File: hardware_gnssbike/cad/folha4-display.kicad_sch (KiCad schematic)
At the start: 11 parts, among them J401 Hirose FH12-10S-0.5SH(55), J402 Molex 503480-0500, Q401 DMG1012T-7

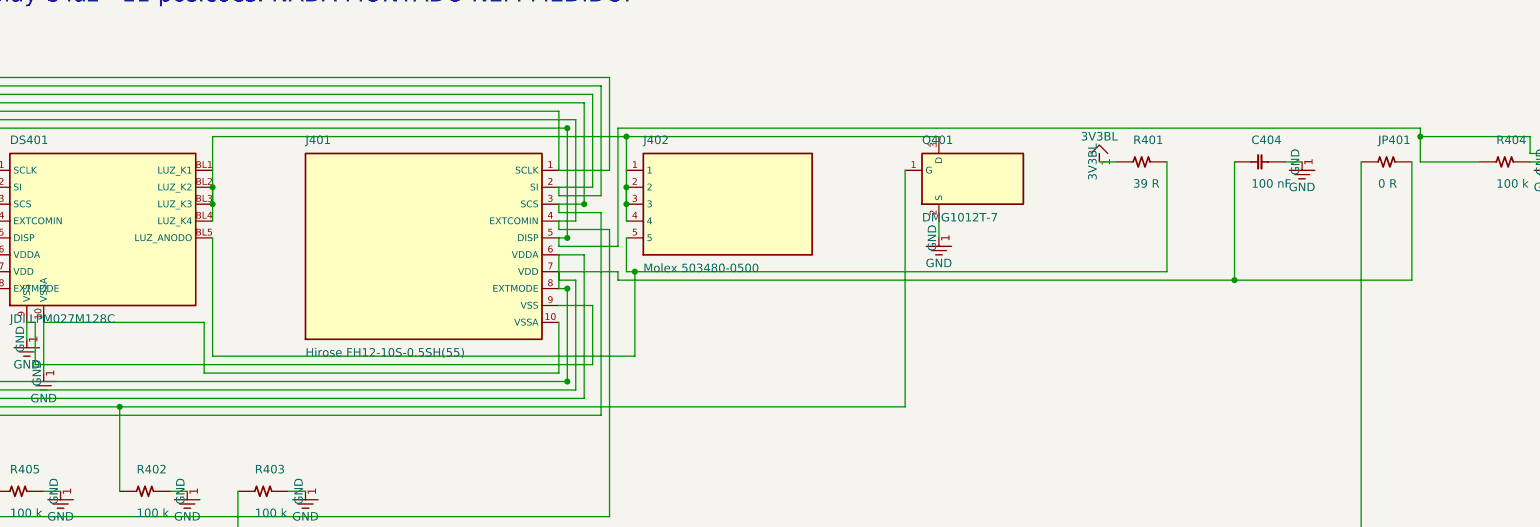
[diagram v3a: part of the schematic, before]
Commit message: feat(hardware): real symbols and real 3D models, from KiCad's own libraries
Two of the owner's asks in one commit, because they turned out to be the
same idea: stop drawing what already exists, reviewed, in the library.

THE SCHEMATIC. 36 of the parts were rectangles with pins around them - the
ICs, the connectors and the display - and a rectangle says nothing. Anyone
reading a schematic recognises a coaxial connector by the circle with the
dot, a switch by the contact that opens, a MOSFET by the channel and the
arrow.

ksym.py reads a symbol out of KiCad's own library - 21.110 of them, every
one reviewed against the KLC - and embeds it in our schematic with our
properties. simbolos.py says which part uses which. Eleven are in, and
ksym.checar() verifies every one pin number by pin number, because a
pretty symbol with the wire on the wrong pin is worse than a correct
rectangle. RF_GPS:MAX-M10S is literally our receiver: 18 pins, 18 names,
the same LCC-18.

Three symbols verify clean and still break the drawing, and they are
parked with the reason MEASURED rather than "did not work": the ADP5091
puts MPPT on the bottom edge beside its three ground pins and the ground
power symbol lands on the MPPT wire; the USB-C stacks four contacts per
point with 5,08 mm stubs and VBUS meets CC1; the ten pins of the display
FPC are all on one edge and two wires cannot reach. Each needs work
somewhere else - the power symbol placer, the placement - not a different
symbol.

Three bugs were found and fixed on the way, all in the router, all of the
same family: it assumed things about symbols that are only true of the
ones this project draws.

  - Symbols from KiCad are NOT centred on their origin. A
    Conn_01x10_Socket has its drawing at x -1,27 to 0 and all ten pins at
    x = -5,08. Treated as centred, pins fall inside the obstacle, the
    router cannot reach them from outside and goes over them instead -
    and two nets that touch are one net, with nothing in the drawing
    sa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
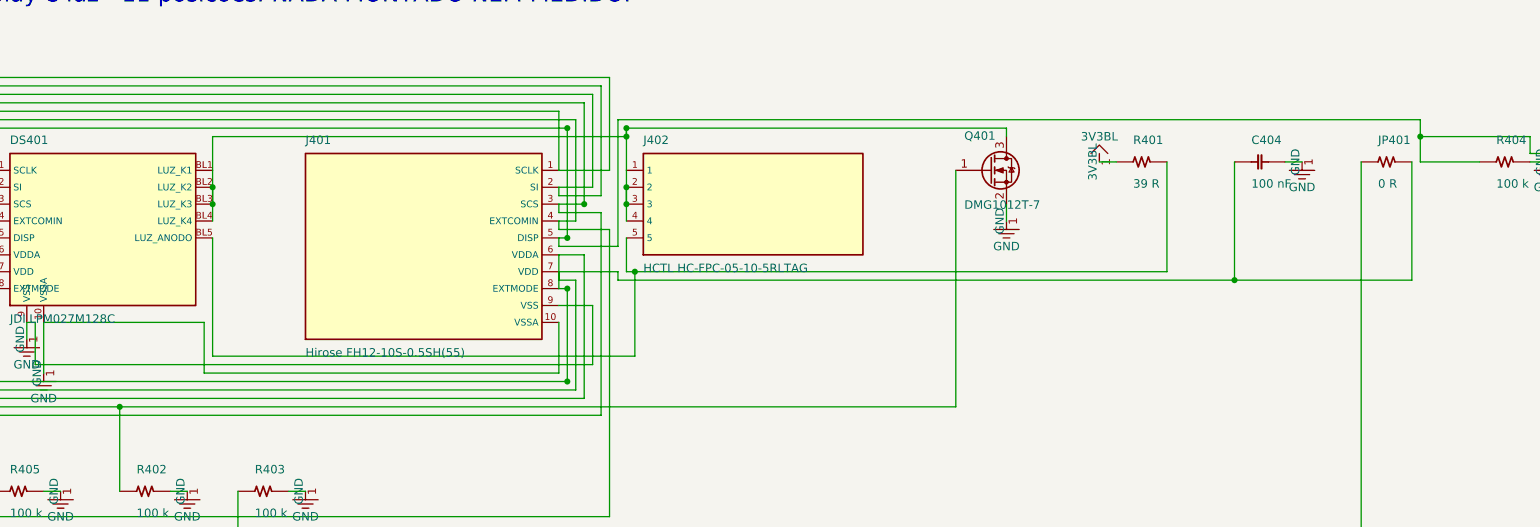
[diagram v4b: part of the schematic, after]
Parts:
- J402: value Molex 503480-0500 -> HCTL HC-FPC-05-10-5RLTAG; footprint Connector_FFC-FPC:TE_0-1734839-5_1x05-1MP_P0.5mm_Horizontal -> gnssbike:HC-FPC-05-10-5RLTAG
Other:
- moved on the sheet: J402
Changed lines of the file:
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@@
 	(wire
 		(pts
-			(xy 171.450 44.450) (xy 171.450 46.990)
+			(xy 181.610 41.910) (xy 181.610 44.450)
 		)
 		(stroke (width 0) (type default))
@@
 	(wire
 		(pts
-			(xy 124.460 31.750) (xy 171.450 31.750)
-		)
-		(stroke (width 0) (type default))
-	)
-	(wire
-		(pts
-			(xy 124.460 31.750) (xy 124.460 36.830)
+			(xy 181.610 30.480) (xy 181.610 31.750)
+		)
+		(stroke (width 0) (type default))
+	)
+	(wire
+		(pts
+			(xy 124.460 30.480) (xy 181.610 30.480)
+		)
+		(stroke (width 0) (type default))
+	)
+	(wire
+		(pts
+			(xy 124.460 31.750) (xy 124.460 30.480)
+		)
+		(stroke (width 0) (type default))
+	)
+	(wire
+		(pts
+			(xy 124.460 30.480) (xy 124.460 36.830)
 		)
 		(stroke (width 0) (type default))
@@
 	(wire
 		(pts
-			(xy 48.260 72.390) (xy 166.370 72.390)
-		)
-		(stroke (width 0) (type default))
-	)
-	(wire
-		(pts
-			(xy 166.370 36.830) (xy 166.370 72.390)
+			(xy 48.260 72.390) (xy 173.990 72.390)
+		)
+		(stroke (width 0) (type default))
+	)
+	(wire
+		(pts
+			(xy 173.990 36.830) (xy 173.990 72.390)
 		)
 		(stroke (width 0) (type default))
@@
 	(wire
 		(pts
-			(xy 243.840 30.480) (xy 243.840 31.750)
+			(xy 243.840 29.210) (xy 243.840 31.750)
 		)
 		(stroke (width 0) (type default))
@@
 	(wire
 		(pts
-			(xy 123.190 30.480) (xy 243.840 30.480)
-		)
-		(stroke (width 0) (type default))
-	)
-	(wire
-		(pts
-			(xy 123.190 30.480) (xy 123.190 48.260)
+			(xy 123.190 29.210) (xy 243.840 29.210)
+		)
+		(stroke (width 0) (type default))
+	)
+	(wire
+		(pts
+			(xy 123.190 29.210) (xy 123.190 48.260)
 		)
 		(stroke (width 0) (type default))
@@
 	(junction
 		(at 124.460 41.910)
+		(diameter 0)
+		(color 0 0 0 0)
+	)
+	(junction
+		(at 124.460 30.480)
 		(diameter 0)
 		(color 0 0 0 0)
@@
 	(symbol
 		(lib_id "gnssbike:J402")
-		(at 139.700 41.910 0)
+		(at 143.510 41.910 0)
 		(unit 1)
 		(exclude_from_sim no)
@@
 			(effects (font (size 1.27 1.27)) (justify left bottom))
 		)
-		(property "Value" "Molex 503480-0500"
+		(property "Value" "HCTL HC-FPC-05-10-5RLTAG"
 			(at 127.000 50.800 0)
 			(effects (font (size 1.27 1.27)) (justify left top))
 		)
-		(property "Footprint" "Connector_FFC-FPC:TE_0-1734839-5_1x05-1MP_P0.5mm_Horizontal"
-			(at 139.7 41.910000000000004 0)
+		(property "Footprint" "gnssbike:HC-FPC-05-10-5RLTAG"
+			(at 143.51 41.910000000000004 0)
 			(effects (font (size 1.27 1.27)) (hide yes))
 		)
 		(property "Datasheet" ""
-			(at 139.7 41.910000000000004 0)
+			(at 143.51 41.910000000000004 0)
 			(effects (font (size 1.27 1.27)) (hide yes))
 		)
 		(property "Description" "conector da luz do painel, 5 vias, passo 0,5 mm, recomendado pela propria JDI no desenho de contorno"
-			(at 139.7 41.910000000000004 0)
+			(at 143.51 41.910000000000004 0)
 			(effects (font (size 1.27 1.27)) (hide yes))
 		)
@@
 	(symbol
 		(lib_id "gnssbike:Q401")
-		(at 176.530 38.100 0)
+		(at 179.070 36.830 0)
 		(unit 1)
 		(exclude_from_sim no)
@@
 		(dnp no)
 		(property "Reference" "Q401"
-			(at 168.910 33.020 0)
+			(at 175.260 32.385 0)
 			(effects (font (size 1.27 1.27)) (justify left bottom))
 		)
 		(property "Value" "DMG1012T-7"
-			(at 168.910 43.180 0)
+			(at 175.260 41.275 0)
 			(effects (font (size 1.27 1.27)) (justify left top))
 		)
 		(property "Footprint" "Package_TO_SOT_SMD:SOT-523"
-			(at 176.53 38.1 0)
+			(at 179.07 36.83 0)
 			(effects (font (size 1.27 1.27)) (hide yes))
 		)
 		(property "Datasheet" ""
-			(at 176.53 38.1 0)
+			(at 179.07 36.83 0)
 			(effects (font (size 1.27 1.27)) (hide yes))
 		)
 		(property "Description" "chave de canal N da luz. A Diodes NAO publica numero de pino: o diagrama so mostra a posicao, e a numeracao vem do padrao SOT-523 | PINAGEM NAO CONFIRMADA NA FICHA"
-			(at 176.53 38.1 0)
+			(at 179.07 36.83 0)
 			(effects (font (size 1.27 1.27)) (hide yes))
 		)
@@
 	(symbol
 		(lib_id "power:GND")
-		(at 171.450 46.990 0)
+		(at 181.610 44.450 0)
 		(unit 1)
 		(exclude_from_sim no)
@@
 		(dnp no)
 		(property "Reference" "#PWR003"
-			(at 171.45 46.99 0)
+			(at 181.61 44.449999999999996 0)
 			(effects (font (size 1.27 1.27)) (hide yes))
 		)
 		(property "Value" "GND"
-			(at 171.450 50.800 0)
+			(at 181.610 48.260 0)
 			(effects (font (size 1.27 1.27)))
 		)
 		(property "Footprint" ""
-			(at 171.45 46.99 0)
+			(at 181.61 44.449999999999996 0)
 			(effects (font (size 1.27 1.27)) (hide yes))
 		)
 		(property "Datasheet" ""
-			(at 171.45 46.99 0)
-			(effects (font (size 1.27 1.27)) (hide yes))
-		)
+			(at 181.61 44.449999999999996 0)
+			(effects (font (size 1.27 1.27)) (hide yes))
+		)

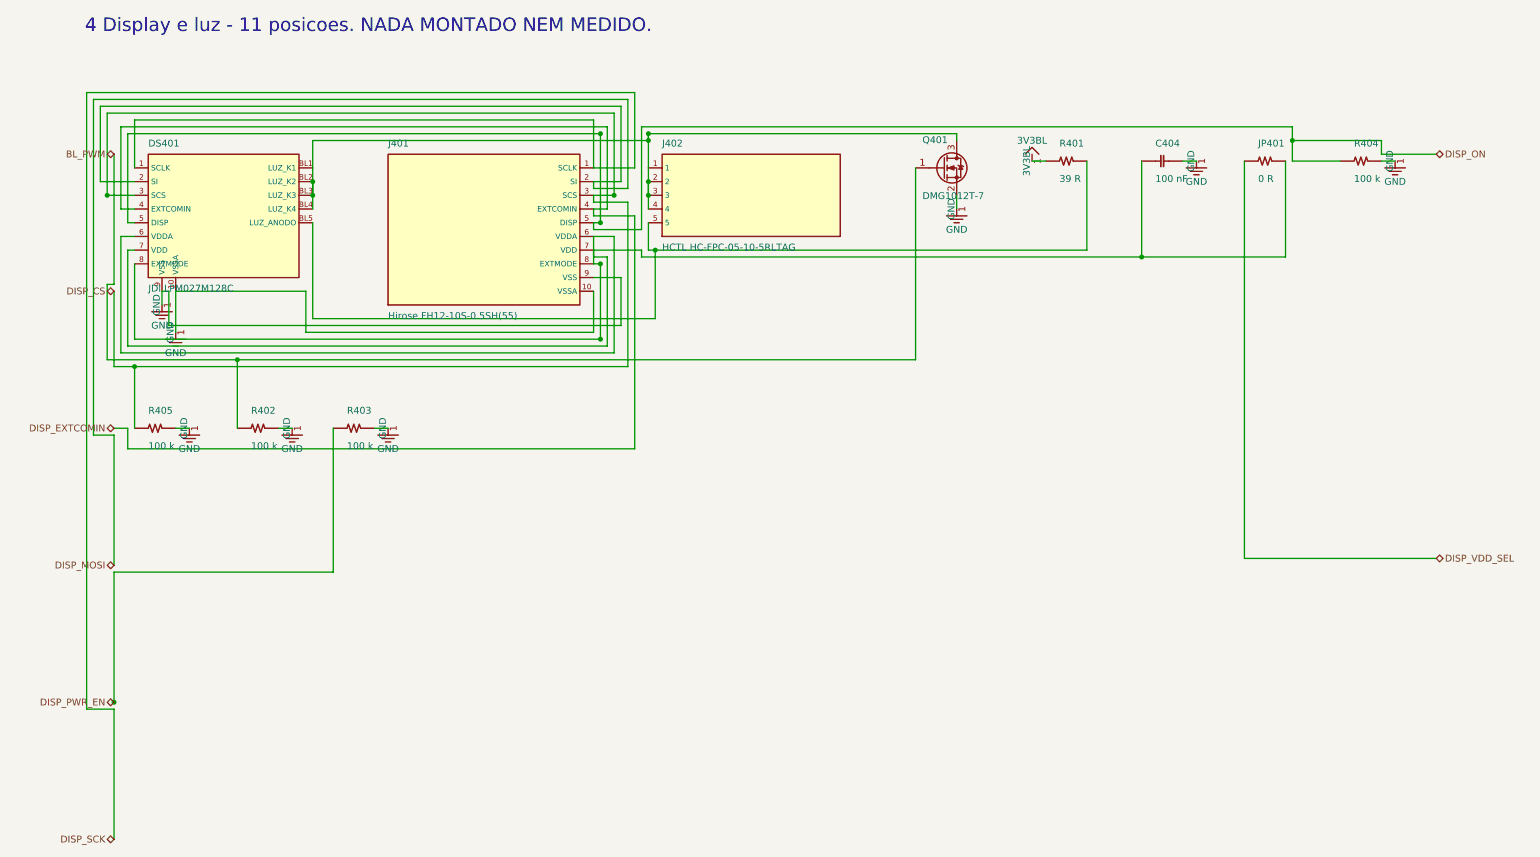
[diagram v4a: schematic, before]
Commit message: fix(hardware): the debug connector had RESET on the wrong contact
This one would have cost a board. The Tag-Connect TC2030 footprint had
pin 3 as no-connect and RESET on pin 6. The manufacturer's own data
sheet, TC2030-CTX_1.pdf, table "Connections", says the opposite: on the
six-pin footprint it is 3 = nRESET and 6 = SWO/TDO.

Where the mistake came from is worth writing down, because it is easy to
make twice: 1 VCC, 2 SWDIO, 3 GND, 4 SWCLK, 5 GND, 6 SWO is the
numbering of the ten-way Cortex header on the PROBE side, not of the
six-pin footprint on the board. Mixing the two gives exactly what was
written here.

What it would have done: the probe's nRESET is an open drain output, so
it would have driven nothing, and the MCU's reset would have hung off
the probe's SWO INPUT. Nothing burns - SWO runs target to probe, there
is no short - but the debugger can never reset the target: no connect
under reset, no pin reset. On an nRF54LM20A that reboots from task_wdt
or reconfigures its SWD pins, that removes the standard way out and
leaves only a full CTRL-AP erase.

The documentation carried a worse version still. 06 had GND on contact 3,
which fabricated would tie the probe's open-drain nRESET to copper
ground and hold the target in reset forever.

The project's own notes had predicted this exact variant - 06 carried a
CAUTION saying so and README an open checklist item. It was that one, and
it was caught before layout. Both are now closed, and the connector's
pin 6 is recorded as SWO with what is still unknown about it: which pad
of the ME54BS13 exposes SWO, which would give printf over ITM during
bring-up.

Fixed in parts.py, nets.py, 03-netlist.md, 06-conectores-e-pontos-de-teste.md,
07-sequencias-e-protecao.md and README.md.

Verified: check_sch and check_pcb pass, 78 of 78 diagrams render, 1529
links and none broken.
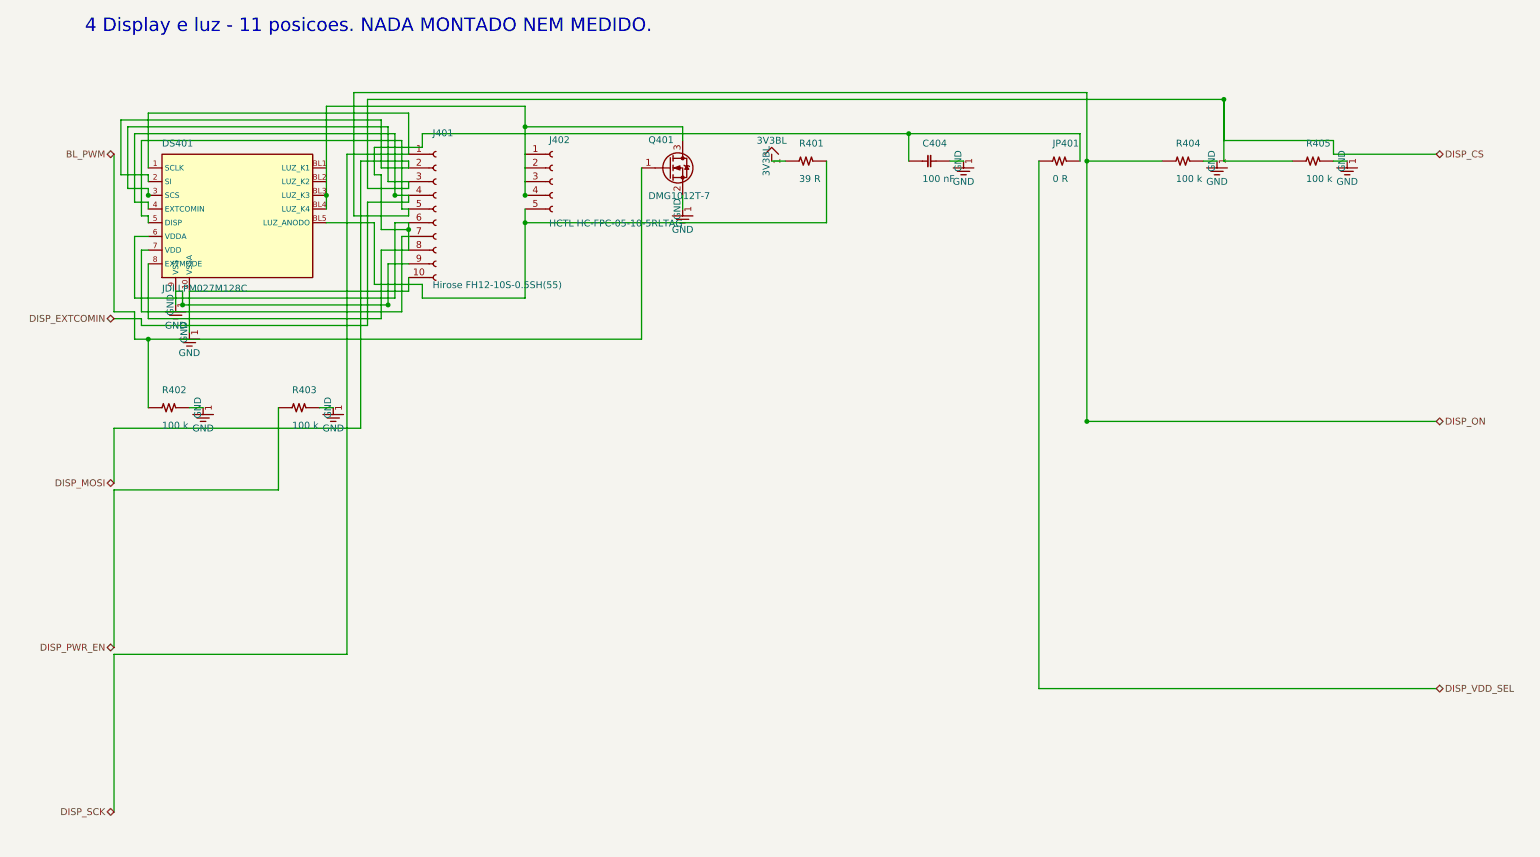
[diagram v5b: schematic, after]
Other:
- moved on the sheet: C404, DS401, JP401, Q401, R401, R402, R403, R404, R405
